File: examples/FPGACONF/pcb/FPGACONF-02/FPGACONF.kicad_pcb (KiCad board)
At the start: 2 copper layers, 85 x 100 mm, 88 parts, among them CN201 CN_20x2_D1.0mm_P2.54mm_TH, CN202 CN_10x2_D1.0mm_P2.54mm_TH, CN203 CN_20x2_D1.0mm_P2.54mm_TH, CN204 CN_02x1_D1.0mm_P2.54mm_TH, CN205 JST_SM04B-SRSS-TB, CN401 JST_SM04B-SRSS-TB, CN402 JST_SM04B-SRSS-TB, CN403 JST_SM04B-SRSS-TB, CN404 ZX62D-B-5PA8(30), CN501 CN_10x2_D1.0mm_P2.54mm_TH, CN502 CN_07x2_D1.0mm_P2.54mm_TH, J501 SD_DM1B-DSF-PEJ, U201 STM32F730Z8T, U202 STM32F730V8T, U301 SN74CBTLV3257D, U401 LP5907MFX-3.3/NOPB, X201 ASVTX-12-A-40.000MHZ-H10-T

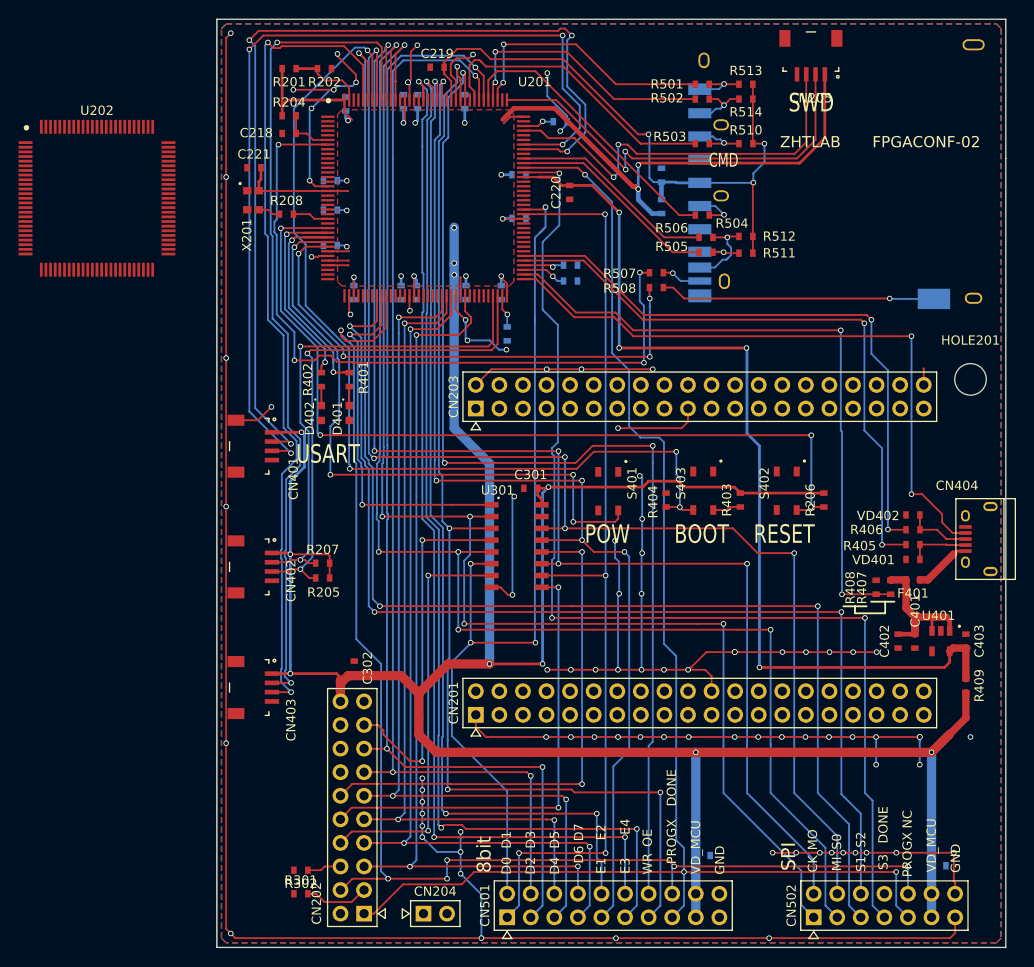
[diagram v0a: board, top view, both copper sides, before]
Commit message: FPGACONF-02 pcb  support for the SD-DDR test
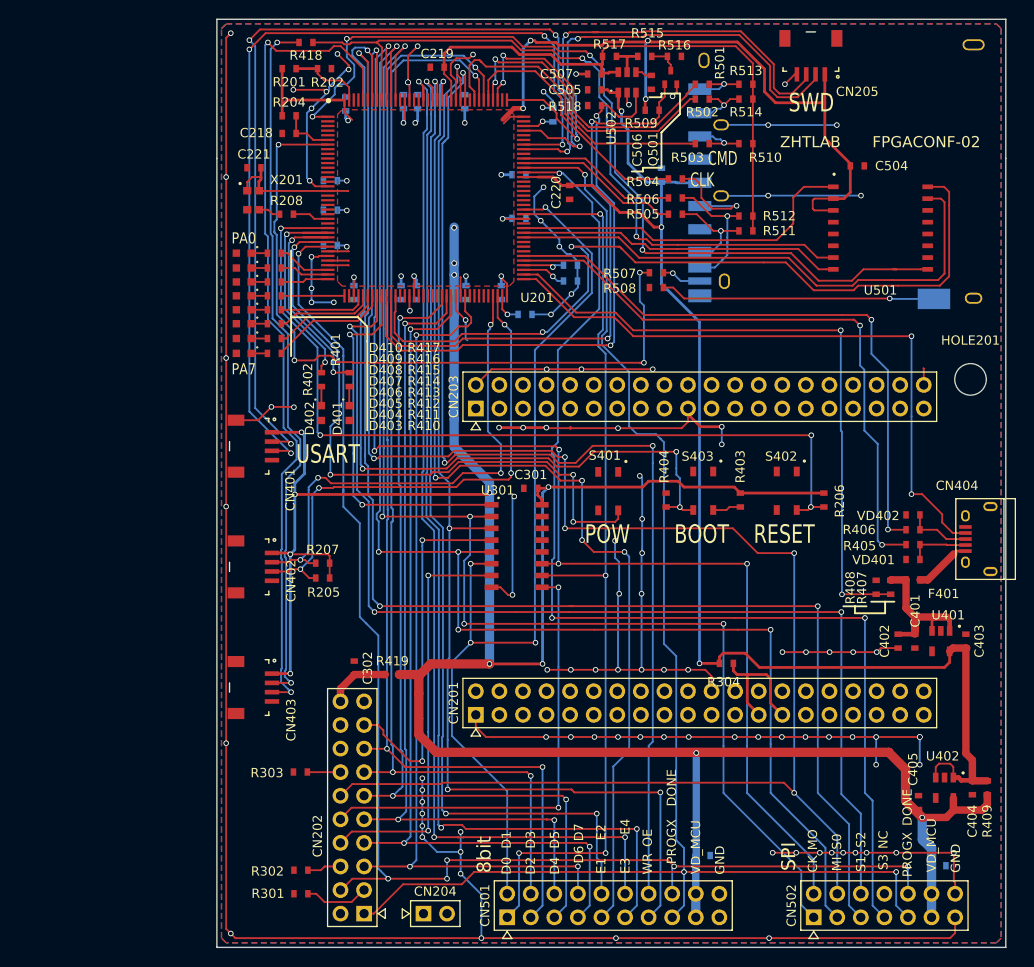
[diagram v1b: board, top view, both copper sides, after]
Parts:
- removed U202: STM32F730V8T, zhtlab_SMD_QFP_QFN:TQFP-100_14x14mm_Pitch0.5mm
- added C404: 1u, zhtlab_SMD_standard:RCL_1608m, F.Cu at (131.4, 97.8)
- added C405: 1u, zhtlab_SMD_standard:RCL_1608m, F.Cu at (125.6, 99.4)
- added C504: 0.1u, zhtlab_SMD_standard:RCL_1608m, F.Cu at (119.0, 30.8)
- added C505: 1u, zhtlab_SMD_standard:RCL_1608m, F.Cu at (90.7, 22.6)
- added C506: 0.01u, zhtlab_SMD_standard:RCL_1608m, F.Cu at (96.8, 21.8)
- added C507: 2.2u, zhtlab_SMD_standard:RCL_1608m, F.Cu at (90.7, 20.9)
- added D403: SML-E12V8TT86, zhtlab_SMD001-010:LED_1608M_Rohm, F.Cu at (52.9, 51.0)
- added D404: SML-E12V8TT86, zhtlab_SMD001-010:LED_1608M_Rohm, F.Cu at (52.9, 49.4)
- added D405: SML-E12V8TT86, zhtlab_SMD001-010:LED_1608M_Rohm, F.Cu at (52.9, 47.8)
- added D406: SML-E12V8TT86, zhtlab_SMD001-010:LED_1608M_Rohm, F.Cu at (52.9, 46.3)
- added D407: SML-E12V8TT86, zhtlab_SMD001-010:LED_1608M_Rohm, F.Cu at (52.9, 44.8)
- added D408: SML-E12V8TT86, zhtlab_SMD001-010:LED_1608M_Rohm, F.Cu at (52.9, 43.3)
- added D409: SML-E12V8TT86, zhtlab_SMD001-010:LED_1608M_Rohm, F.Cu at (52.9, 41.8)
- added D410: SML-E12V8TT86, zhtlab_SMD001-010:LED_1608M_Rohm, F.Cu at (52.9, 40.2)
- added Q501: RU1C001UN, zhtlab_SMD_standard:SC-85_2.0x2.0mm, F.Cu at (98.9, 22.0)
- added R303: 0, zhtlab_SMD_standard:RCL_1608m, F.Cu at (59.0, 96.1)
- added R304: 0, zhtlab_SMD_standard:RCL_1608m, F.Cu at (104.9, 84.4)
- added R410: 4.7k, zhtlab_SMD_standard:RCL_1608m, F.Cu at (56.2, 51.0)
- added R411: 4.7k, zhtlab_SMD_standard:RCL_1608m, F.Cu at (56.2, 49.4)
- added R412: 4.7k, zhtlab_SMD_standard:RCL_1608m, F.Cu at (56.2, 47.8)
- added R413: 4.7k, zhtlab_SMD_standard:RCL_1608m, F.Cu at (56.2, 46.3)
- added R414: 4.7k, zhtlab_SMD_standard:RCL_1608m, F.Cu at (56.2, 44.8)
- added R415: 4.7k, zhtlab_SMD_standard:RCL_1608m, F.Cu at (56.2, 43.3)
- added R416: 4.7k, zhtlab_SMD_standard:RCL_1608m, F.Cu at (56.2, 41.8)
- added R417: 4.7k, zhtlab_SMD_standard:RCL_1608m, F.Cu at (56.2, 40.2)
- added R418: 22, zhtlab_SMD_standard:RCL_1608m, F.Cu at (59.6, 17.5)
- added R419: 0, zhtlab_SMD_standard:RCL_1608m, F.Cu at (68.9, 85.6)
- added R515: 7.5k, zhtlab_SMD_standard:RCL_1608m, F.Cu at (96.1, 19.0)
- added R516: 20k, zhtlab_SMD_standard:RCL_1608m, F.Cu at (99.3, 19.0)
- added R517: 13k, zhtlab_SMD_standard:RCL_1608m, F.Cu at (92.3, 19.0)
- added R518: 100k, zhtlab_SMD_standard:RCL_1608m, F.Cu at (90.7, 24.3)
- added U402: LP5907MFX-1.8/NOPB, zhtlab_SMD_standard:SOT-23-5_2.7x2.9mm_Pitch0.95mm, F.Cu at (128.4, 97.8)
- added U501: MT25QL01GBBB8ESF-0SIT, zhtlab_SMD_standard:SOIC-16_10.3x10.3mm_Pitch1.27mm, F.Cu at (121.5, 37.5)
- added U502: TPS73001DBVR, zhtlab_SMD_standard:SOT-23-6_2.7x2.9mm_Pitch0.95mm, F.Cu at (94.2, 21.8)
- C301: value 2.2u -> 0.1u
- R509: value 0 -> 100k; moved to F.Cu
- moved R409 11.2 mm to (133.0, 97.8)
- moved R509 10.4 mm to (96.9, 24.8), turned to 180 degrees
- moved R506 5.38 mm to (99.4, 34.2)
- moved R505 5.26 mm to (99.4, 36.0)
- moved R504 4.86 mm to (99.4, 32.2)
- moved C204 2.84 mm to (83.2, 46.8), turned to 180 degrees
- moved R511 2.40 mm to (107.0, 37.8)
- moved R512 2.20 mm to (107.0, 36.2)
- moved C203 1.08 mm to (86.2, 25.3), turned to 270 degrees
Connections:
- net MCU_PB13:USB_ID renamed MCU_PB12:USB_ID
- net MCU_PC3:USB_VBUS_EN renamed MCU_PB13:USB_VBUS_EN
- C219 pad 2: VD3P30_SD -> VD_SDIO
- C220 pad 2: VD3P30_USB -> VD3P30
- C302 pad 2: VD_MCU -> VD_VCCIO8
- C403 pad 2: VD3P30_USB -> VD3P30
- C501 pad 2: VD3P30_SD -> VD3P30
- CN201 pad 25: (no net) -> Net-(CN201-Pad25)
- CN201 pad 27: (no net) -> Net-(CN201-Pad25)
- CN202 pad 12: FPGA_CSX -> MCU_PB7:SPI1_CS0X
- CN202 pad 14: (no net) -> Net-(CN202-Pad14)
- CN202 pad 20: VD_MCU -> VD_VCCIO8
- CN202 pad 4: MCU_PB0:FPGA_DONE -> MCU_PC3:FPGA_DONE
- CN403 pad 2: MCU_PB6:I2CS_SCL -> Net-(CN403-Pad2)
- CN501 pad 16: MCU_PB0:FPGA_DONE -> MCU_PC3:FPGA_DONE
- CN502 pad 10: MCU_PB0:FPGA_DONE -> MCU_PC3:FPGA_DONE
- J501 pad 4: VD3P30_SD -> VD3P30
- R409 pad 1: VD3P30_USB -> VD3P30
- R508 pad 1: MCU_PC3:SDMMC1_WP_X -> (no net)
- R509 pad 1: VD3P30_SD -> MCU_PB1:SDMMC1_VSEL33
- R510 pad 2: VD3P30_SD -> VD_SDIO
- R511 pad 2: VD3P30_SD -> VD_SDIO
- R512 pad 2: VD3P30_SD -> VD_SDIO
- R513 pad 2: VD3P30_SD -> VD_SDIO
- R514 pad 2: VD3P30_SD -> VD_SDIO
- U201 pad 1: (no net) -> MCU_PE2:QSPI_D2
- U201 pad 121: VD3P30_SD -> VD_SDIO
- U201 pad 136: MCU_PB6:I2CS_SCL -> MCU_PB6:I2CS_SCL_QSPI_CSX
- U201 pad 29: MCU_PC3:SDMMC1_WP_X -> MCU_PC3:FPGA_DONE
- U201 pad 34: (no net) -> MCU_PA0:LED0
- U201 pad 35: (no net) -> MCU_PA1:LED1
- U201 pad 36: (no net) -> MCU_PA2:LED2
- U201 pad 37: (no net) -> MCU_PA3:LED3
- U201 pad 40: (no net) -> MCU_PA4:LED4
- U201 pad 41: (no net) -> MCU_PA5:LED5
- U201 pad 42: (no net) -> MCU_PA6:LED6
- U201 pad 43: (no net) -> MCU_PA7:LED7
- U201 pad 46: MCU_PB0:FPGA_DONE -> MCU_PB0:SDMMC1_PWREN
- U201 pad 47: (no net) -> MCU_PB1:SDMMC1_VSEL33
- U201 pad 48: (no net) -> MCU_PB2:QSPI_CLK
- U201 pad 82: (no net) -> MCU_PD11:QSPI_D0
- U201 pad 83: (no net) -> MCU_PD12:QSPI_D1
- U201 pad 84: (no net) -> MCU_PD13:QSPI_D3
- U201 pad 95: VD3P30_USB -> VD3P30
- U301 pad 12: FPGA_CSX -> ~
- U301 pad 13: MCU_PD7:FMC_NE1 -> (no net)
- U301 pad 14: MCU_PB7:SPI1_CS0X -> (no net)
- U401 pad 5: VD3P30_USB -> VD3P30
- X201 pad 1: (no net) -> VD_MCU
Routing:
- net VD3P30: track 0.00 -> 145.6 mm, vias 0 -> 3
- net MCU_PC3:FPGA_DONE: track 0.00 -> 145.1 mm, vias 0 -> 6
- net MCU_PB0:FPGA_DONE: track 140.8 -> 0.00 mm, vias 6 -> 0
- net VD3P30_USB: track 102.8 -> 0.00 mm, vias 4 -> 0
- net MCU_PE2:QSPI_D2: track 0.00 -> 96.3 mm, vias 0 -> 4
- net MCU_PB6:I2CS_SCL: track 91.0 -> 0.00 mm, vias 2 -> 0
- net MCU_PB2:QSPI_CLK: track 0.00 -> 89.1 mm, vias 0 -> 2
- net MCU_PB6:I2CS_SCL_QSPI_CSX: track 0.00 -> 80.5 mm, vias 0 -> 2
- net Net-(CN403-Pad2): track 0.00 -> 76.1 mm, vias 0 -> 2
- net VD3P30_SD: track 69.7 -> 0.00 mm, vias 3 -> 0
- net MCU_PB1:SDMMC1_VSEL33: track 0.00 -> 64.2 mm, vias 0 -> 2
- net MCU_PB0:SDMMC1_PWREN: track 0.00 -> 63.3 mm, vias 0 -> 2
- net VD_SDIO: track 0.00 -> 63.1 mm
- net ~: track 466.1 -> 527.4 mm, vias 90 -> 107
- net MCU_PD11:QSPI_D0: track 0.00 -> 58.0 mm
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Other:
- board text added: "CLK"
- board text added: "PA0"
- board text added: "PA7"
